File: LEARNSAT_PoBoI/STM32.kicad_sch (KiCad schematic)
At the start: 24 parts, among them U17 LP5907SNX-3.3, U21 74AC14MTCX, U22 LTC4304CMS#PBF, U26 ISL3259EIRZ, U6 STM32F103RET6, Y1 ABS07-166-32.768KHZ-T

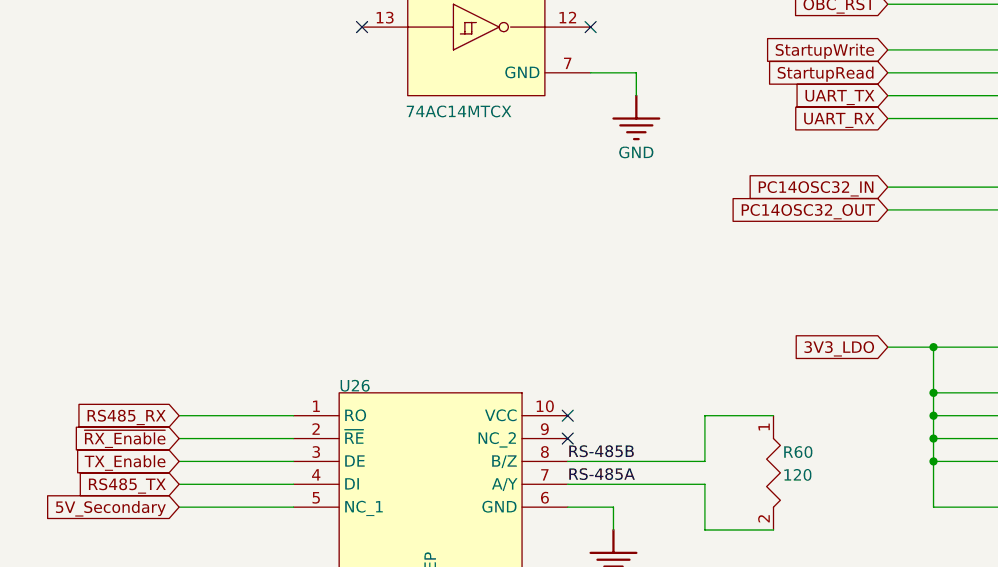
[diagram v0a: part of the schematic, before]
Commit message: Edited 12V Rail schematics
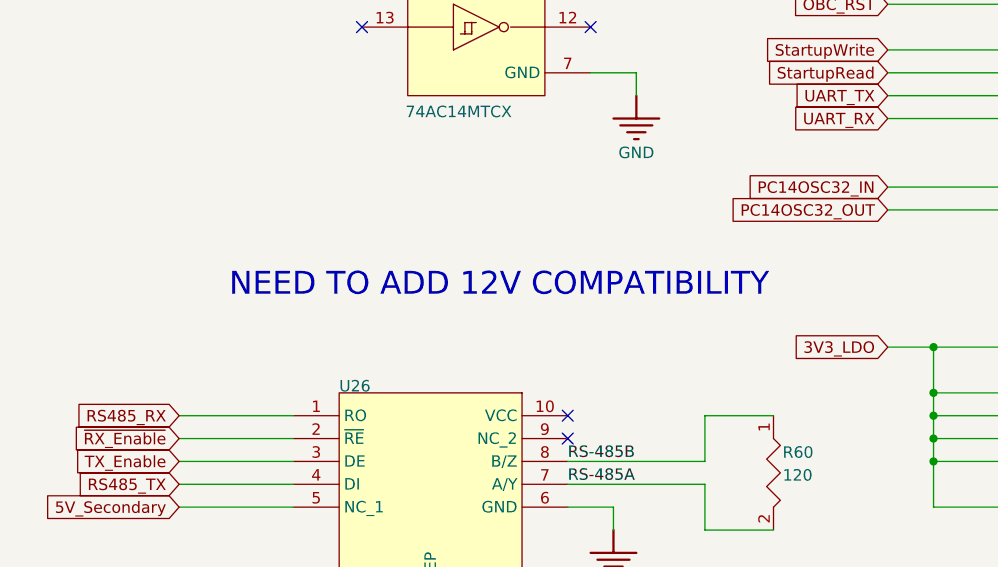
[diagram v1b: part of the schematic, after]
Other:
- note added: "NEED TO ADD 12V COMPATIBILITY"
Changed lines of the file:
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@@
+		)
+	)
+	(text "NEED TO ADD 12V COMPATIBILITY"
+		(exclude_from_sim no)
+		(at 45.72 135.382 0)
+		(effects
+			(font
+				(size 2.54 2.54)
+			)
 		)
 	)
